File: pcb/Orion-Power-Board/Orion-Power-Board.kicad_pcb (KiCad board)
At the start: 2 copper layers, 0 parts

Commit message: Done layout of power board
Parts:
- added BT1: 2S_FRONT_LI-ION_BATT, AA_Custom_Components:PowerPad_Pair_5.0x5.0mm_2ndPadFlipped, F.Cu at (120.5, 111.0)
- added BT2: 2S_BACK_LI-ION_BATT, AA_Custom_Components:PowerPad_Pair_5.0x5.0mm_2ndPadFlipped, F.Cu at (179.5, 112.0)
- added C5: 470uF_CAP, Capacitor_THT:CP_Radial_D8.0mm_P3.50mm, F.Cu at (130.0, 89.5)
- added C6: 470uF_CAP, Capacitor_THT:CP_Radial_D8.0mm_P3.50mm, F.Cu at (130.0, 98.5)
- added C7: 470uF_CAP, Capacitor_THT:CP_Radial_D8.0mm_P3.50mm, F.Cu at (170.0, 85.8)
- added C8: 470uF_CAP, Capacitor_THT:CP_Radial_D8.0mm_P3.50mm, F.Cu at (170.0, 94.8)
- added G***: LOGO, Orion-Logo:Orion-Logo-20mm, F.Cu at (167.0, 77.5)
- added H1: MountingHole, MountingHole:MountingHole_3.2mm_M3_Pad, F.Cu at (118.5, 80.0)
- added H2: MountingHole, MountingHole:MountingHole_3.2mm_M3_Pad, F.Cu at (180.5, 80.0)
- added H3: MountingHole, MountingHole:MountingHole_3.2mm_M3_Pad, F.Cu at (118.5, 125.0)
- added H4: MountingHole, MountingHole:MountingHole_3.2mm_M3_Pad, F.Cu at (180.5, 125.0)
- added J2: 2S_FRONT_BATTERY_BALANCE_HEADER, AA_Custom_Components:JST_XH_1x03_P2.54mm_Vertical, F.Cu at (131.0, 106.9)
- added J3: 2S_BACK_BATTERY_BALANCE_HEADER, AA_Custom_Components:JST_XH_1x03_P2.54mm_Vertical, F.Cu at (167.0, 112.0)
- added J4: 3S_BATTERY_BALANCE_HEADER, AA_Custom_Components:JST_XH_1x04_P2.54mm_Vertical, F.Cu at (163.5, 120.5)
- added J5: 3S_LI-ION_VOLTAGE_ALARM, AA_Custom_Components:LIPO_VOLTAGE_ALARM, F.Cu at (159.2, 82.0)
- added J6: 2S_BACK_LI-ION_VOLTAGE_ALARM, AA_Custom_Components:LIPO_VOLTAGE_ALARM, F.Cu at (156.0, 111.6)
- added J7: 2S_FRONT_LI-ION_VOLTAGE_ALARM, AA_Custom_Components:LIPO_VOLTAGE_ALARM, F.Cu at (142.0, 91.4)
- added J8: CONN_20_POS_KEYED_SOCKET, AA_Custom_Components:SULLINS_SBH11-PBPC-D10-ST-BK_SOCKET, F.Cu at (141.8, 122.3)
- added U1: BACK_6x3_SERVO_HEADER_PIN, AA_Custom_Components:Servo_PinHeader_3x06_P2.54mm_Vertical, F.Cu at (176.4, 86.4)
- added U2: FRONT_6x3_SERVO_HEADER_PIN, AA_Custom_Components:Servo_PinHeader_3x06_P2.54mm_Vertical, F.Cu at (123.5, 98.3)
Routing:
- added copper zone on B.Cu, net +7.4V_BACK_BATT
- added copper zone on B.Cu, net +7.4V_FRONT_BATT
- added copper zone on F.Cu, net GND
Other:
- board outline added: 72 x 55 mm

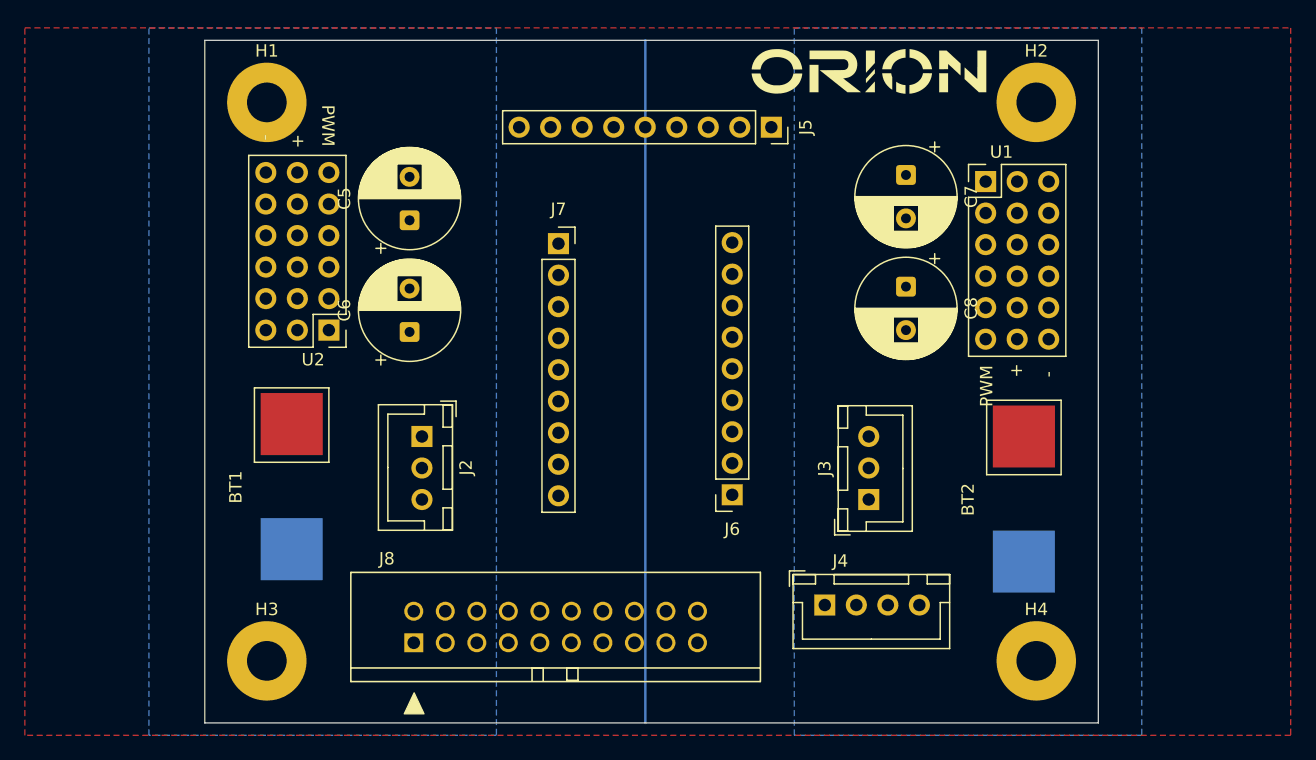
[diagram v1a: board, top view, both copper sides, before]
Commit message: Update power board
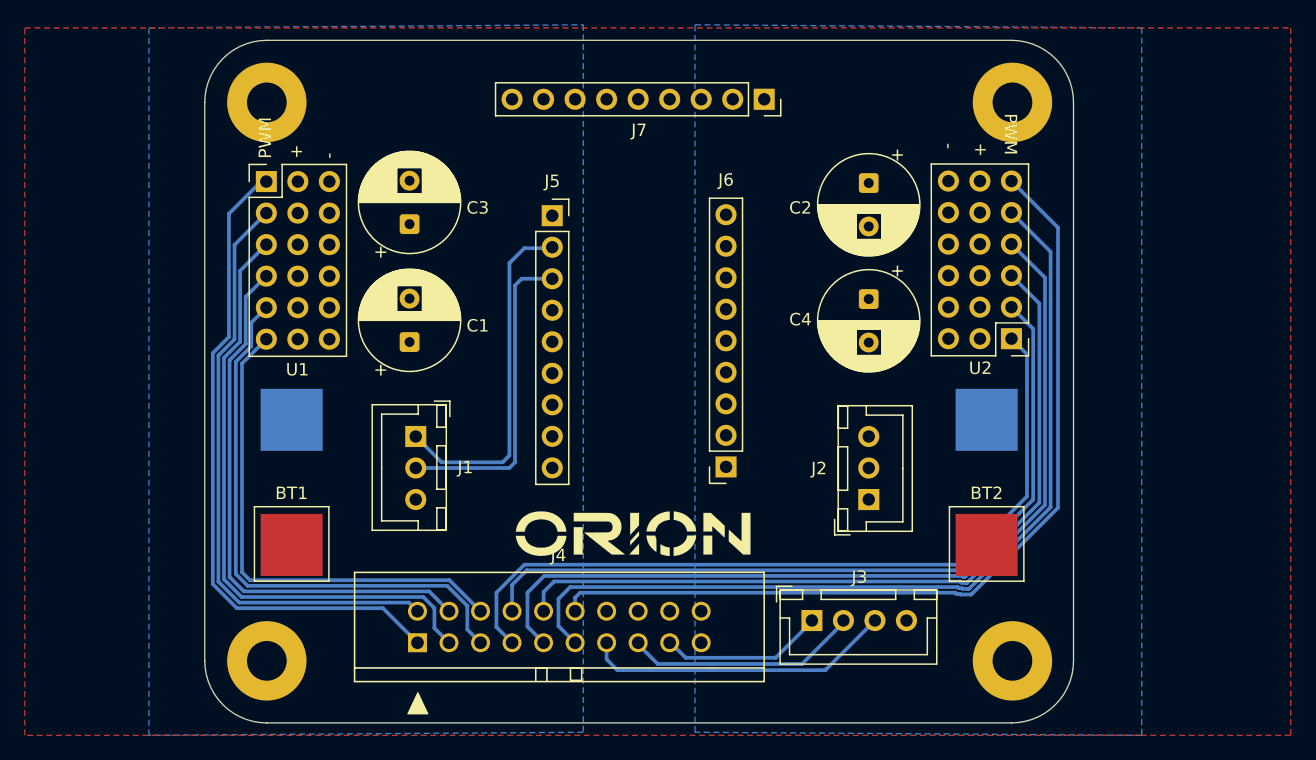
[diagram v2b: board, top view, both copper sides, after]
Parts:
- removed G***: LOGO, Orion-Logo:Orion-Logo-20mm
- added N1: ORION_LOGO, Orion-Logo:Orion-Logo-20mm, F.Cu at (148.0, 114.8)
- moved U1 13.0 mm to (118.5, 86.4), turned to 0 degrees
- moved U2 12.8 mm to (178.5, 99.0), turned to 180 degrees
- moved BT2 3.32 mm to (176.5, 110.6), turned to -90 degrees
- moved C4 3.16 mm to (167.0, 95.8)
- moved C2 3.07 mm to (167.0, 86.5)
- moved J7 2.32 mm to (158.6, 79.8)
- moved J5 2.30 mm to (141.5, 89.1)
- moved J6 2.30 mm to (155.5, 109.4)
- moved H2 1.92 mm to (178.6, 80.0)
- moved H4 1.92 mm to (178.6, 125.0)
- moved J3 1.63 mm to (162.4, 121.8)
- moved C1 0.81 mm to (130.0, 99.3)
- moved J1 0.50 mm to (130.5, 106.9)
- moved BT1 0.42 mm to (120.5, 110.6), turned to -90 degrees
- moved C3 0.31 mm to (130.0, 89.8)
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- renumbered C6 to C1, C7 to C2, C5 to C3, C8 to C4, J2 to J1, J3 to J2, J4 to J3, J8 to J4, J7 to J5, J5 to J7, U2 to U1, U1 to U2
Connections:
- J4 pad 13: 3S_BATT_CELL1 -> 3S_BATT_CELL3
- J4 pad 14: 2S_BATT_REAR_CELL1 -> 2S_BATT_FRONT_CELL1
- J4 pad 16: 2S_BATT_REAR_CELL2 -> 2S_BATT_FRONT_CELL2
- J4 pad 17: 3S_BATT_CELL3 -> 3S_BATT_CELL1
- J4 pad 18: 2S_BATT_FRONT_CELL1 -> 2S_BATT_REAR_CELL2
- J4 pad 20: 2S_BATT_FRONT_CELL2 -> 2S_BATT_REAR_CELL1
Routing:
- net PWM10: track 0.00 -> 72.0 mm
- net PWM11: track 0.00 -> 71.0 mm
- net PWM8: track 0.00 -> 68.1 mm
- net PWM9: track 0.00 -> 67.1 mm
- net PWM6: track 0.00 -> 63.7 mm
- net PWM7: track 0.00 -> 63.2 mm
- net PWM0: track 0.00 -> 52.9 mm
- net PWM2: track 0.00 -> 49.7 mm
- net PWM1: track 0.00 -> 48.3 mm
- net PWM4: track 0.00 -> 45.6 mm
- net PWM3: track 0.00 -> 44.3 mm
- net PWM5: track 0.00 -> 40.1 mm
- net 2S_BATT_FRONT_CELL1: track 0.00 -> 28.2 mm
- net 2S_BATT_FRONT_CELL2: track 0.00 -> 25.7 mm
- net 3S_BATT_CELL3: track 0.00 -> 25.0 mm
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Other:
- board size 72 x 55 mm -> 70 x 55 mm

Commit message: Almost finished power board
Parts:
- added kibuzzard-693F3101: G***, kibuzzard-693F3101, F.Cu at (129.2, 79.8)
- added kibuzzard-693F310D: G***, kibuzzard-693F310D, F.Cu at (167.8, 79.5)
- added kibuzzard-693F3E2A: G***, kibuzzard-693F3E2A, F.Cu at (148.8, 84.9)
- added kibuzzard-693F3F14: G***, kibuzzard-693F3F14, F.Cu at (166.6, 126.3)
- added kibuzzard-693F3F70: G***, kibuzzard-693F3F70, F.Cu at (141.8, 127.7)
- added kibuzzard-693F4000: G***, kibuzzard-693F4000, F.Cu at (130.4, 103.1)
- added kibuzzard-693F4008: G***, kibuzzard-693F4008, F.Cu at (167.2, 103.2)
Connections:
- J4 pad 14: 2S_BATT_FRONT_CELL1 -> 2S_BATT_FRONT_CELL2
- J4 pad 16: 2S_BATT_FRONT_CELL2 -> 2S_BATT_FRONT_CELL1
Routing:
- net 2S_BATT_FRONT_CELL1: track 28.2 -> 103.0 mm, vias 0 -> 6
- net 3S_BATT_CELL3: track 25.0 -> 95.8 mm, vias 0 -> 2
- net 2S_BATT_FRONT_CELL2: track 25.7 -> 96.5 mm, vias 0 -> 6
- net 3S_BATT_CELL2: track 18.9 -> 88.3 mm, vias 0 -> 2
- net 3S_BATT_CELL1: track 13.3 -> 82.2 mm, vias 0 -> 2
- net 2S_BATT_REAR_CELL2: track 0.00 -> 56.2 mm, vias 0 -> 2
- net 2S_BATT_REAR_CELL1: track 0.00 -> 49.3 mm, vias 0 -> 2
- net PWM11: track 71.0 -> 73.4 mm
- net PWM10: track 72.0 -> 74.2 mm
- net PWM9: track 67.1 -> 68.6 mm
- net PWM8: track 68.1 -> 69.3 mm
- net PWM1: track 48.3 -> 47.3 mm
- net PWM6: track 63.7 -> 64.6 mm
- net PWM4: track 45.6 -> 44.8 mm
- net PWM0: track 52.9 -> 52.1 mm
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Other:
- board text added: "+7.4V"
- board text added: "0"
- board text added: "1"
- board text added: "10"
- board text added: "11"
- board text added: "2"
- board text added: "3"
- board text added: "4"
- board text added: "5"
- board text added: "6"
- board text added: "7"
- board text added: "8"
- board text added: "9"
- board text added: "Author: Ashish Agrahari Orion Power Board v1.0"
- board text added: "BT1"
- board text added: "BT2"
- board text added: "GND"

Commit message: Finished power board
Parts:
- removed kibuzzard-693F4000: G***, kibuzzard-693F4000
- removed kibuzzard-693F4008: G***, kibuzzard-693F4008
- added kibuzzard-693F552C: G***, kibuzzard-693F552C, F.Cu at (167.6, 102.9)
- added kibuzzard-693F5536: G***, kibuzzard-693F5536, F.Cu at (130.0, 102.9)
- added kibuzzard-693F656E: G***, kibuzzard-693F656E, F.Cu at (148.2, 97.0)
- added kibuzzard-693F65FC: G***, kibuzzard-693F65FC, F.Cu at (125.0, 76.8)
- moved J3 9.60 mm to (171.7, 124.2), turned to 180 degrees
- moved kibuzzard-693F3E2A 8.41 mm to (148.5, 76.5)
- moved kibuzzard-693F3F14 2.27 mm to (168.1, 128.0)
- moved kibuzzard-693F3F70 0.71 mm to (141.9, 128.4)
- moved kibuzzard-693F310D 0.25 mm to (167.8, 79.8)
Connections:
- BT2 pad 1: +7.4V_BACK_BATT -> +7.4V_REAR_BATT
- C1 pad 1: GND -> +7.4V_FRONT_BATT
- C1 pad 2: +7.4V_FRONT_BATT -> GND
- C2 pad 1: GND -> +7.4V_REAR_BATT
- C2 pad 2: +7.4V_BACK_BATT -> GND
- C3 pad 1: GND -> +7.4V_FRONT_BATT
- C3 pad 2: +7.4V_FRONT_BATT -> GND
- C4 pad 1: GND -> +7.4V_REAR_BATT
- C4 pad 2: +7.4V_BACK_BATT -> GND
- J1 pad 1: 2S_BATT_FRONT_CELL1 -> 2S_BATT_FRONT_CELL2
- J1 pad 2: 2S_BATT_FRONT_CELL2 -> 2S_BATT_FRONT_CELL1
- J2 pad 1: 2S_BATT_REAR_CELL1 -> 2S_BATT_REAR_CELL2
- J2 pad 2: 2S_BATT_REAR_CELL2 -> 2S_BATT_REAR_CELL1
- J3 pad 1: 3S_BATT_CELL1 -> 3S_BATT_CELL3
- J3 pad 3: 3S_BATT_CELL3 -> 3S_BATT_CELL1
- U2 pad 10: +7.4V_BACK_BATT -> +7.4V_REAR_BATT
- U2 pad 11: +7.4V_BACK_BATT -> +7.4V_REAR_BATT
- U2 pad 12: +7.4V_BACK_BATT -> +7.4V_REAR_BATT
- U2 pad 7: +7.4V_BACK_BATT -> +7.4V_REAR_BATT
- U2 pad 8: +7.4V_BACK_BATT -> +7.4V_REAR_BATT
- U2 pad 9: +7.4V_BACK_BATT -> +7.4V_REAR_BATT
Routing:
- net 2S_BATT_REAR_CELL1: track 49.3 -> 55.5 mm
- net 2S_BATT_FRONT_CELL2: track 96.5 -> 101.6 mm
- net 2S_BATT_REAR_CELL2: track 56.2 -> 51.7 mm
- net 3S_BATT_CELL1: track 82.2 -> 84.7 mm
- net 3S_BATT_CELL3: track 95.8 -> 98.1 mm
- net 3S_BATT_CELL2: track 88.3 -> 90.5 mm
- net 2S_BATT_FRONT_CELL1: track 103.0 -> 100.8 mm
- added copper zone on B.Cu, net +7.4V_REAR_BATT
- removed copper zone on B.Cu, net +7.4V_BACK_BATT
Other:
- board text added: "By: Ashish Agrahari"
- board text removed: "Author: Ashish Agrahari Orion Power Board v1.0"
- board text removed: "BT1"
- board text removed: "BT2"

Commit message: Review Power board.
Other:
- board text added: "JLCJLCJLCJLC"
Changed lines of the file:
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@@
 			(net 1 "GND")
 			(pinfunction "19")
-			(pintype "power_in")
+			(pintype "bidirectional")
 			(solder_mask_margin 0.102)
 		)
@@
 				(font
 					(size 0.001 0.001)
+					(thickness 0.15)
 				)
 			)
@@
 				(font
 					(size 0.001 0.001)
+					(thickness 0.15)
 				)
 			)
@@
 				(font
 					(size 0.001 0.001)
+					(thickness 0.15)
 				)
 			)
@@
 				(font
 					(size 0.001 0.001)
+					(thickness 0.15)
 				)
 			)
@@
 		(layer "B.SilkS")
 		(effects
+			(font
+				(size 1 1)
+				(thickness 0.153)
+			)
+			(justify left bottom mirror)
+		)
+	)
+	(gr_text "JLCJLCJLCJLC"
+		(at 174.075 128.625 0)
+		(layer "B.SilkS")
+		(effects
